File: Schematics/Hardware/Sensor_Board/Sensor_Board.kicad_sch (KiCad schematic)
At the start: 90 parts, among them J3 Conn_01x14

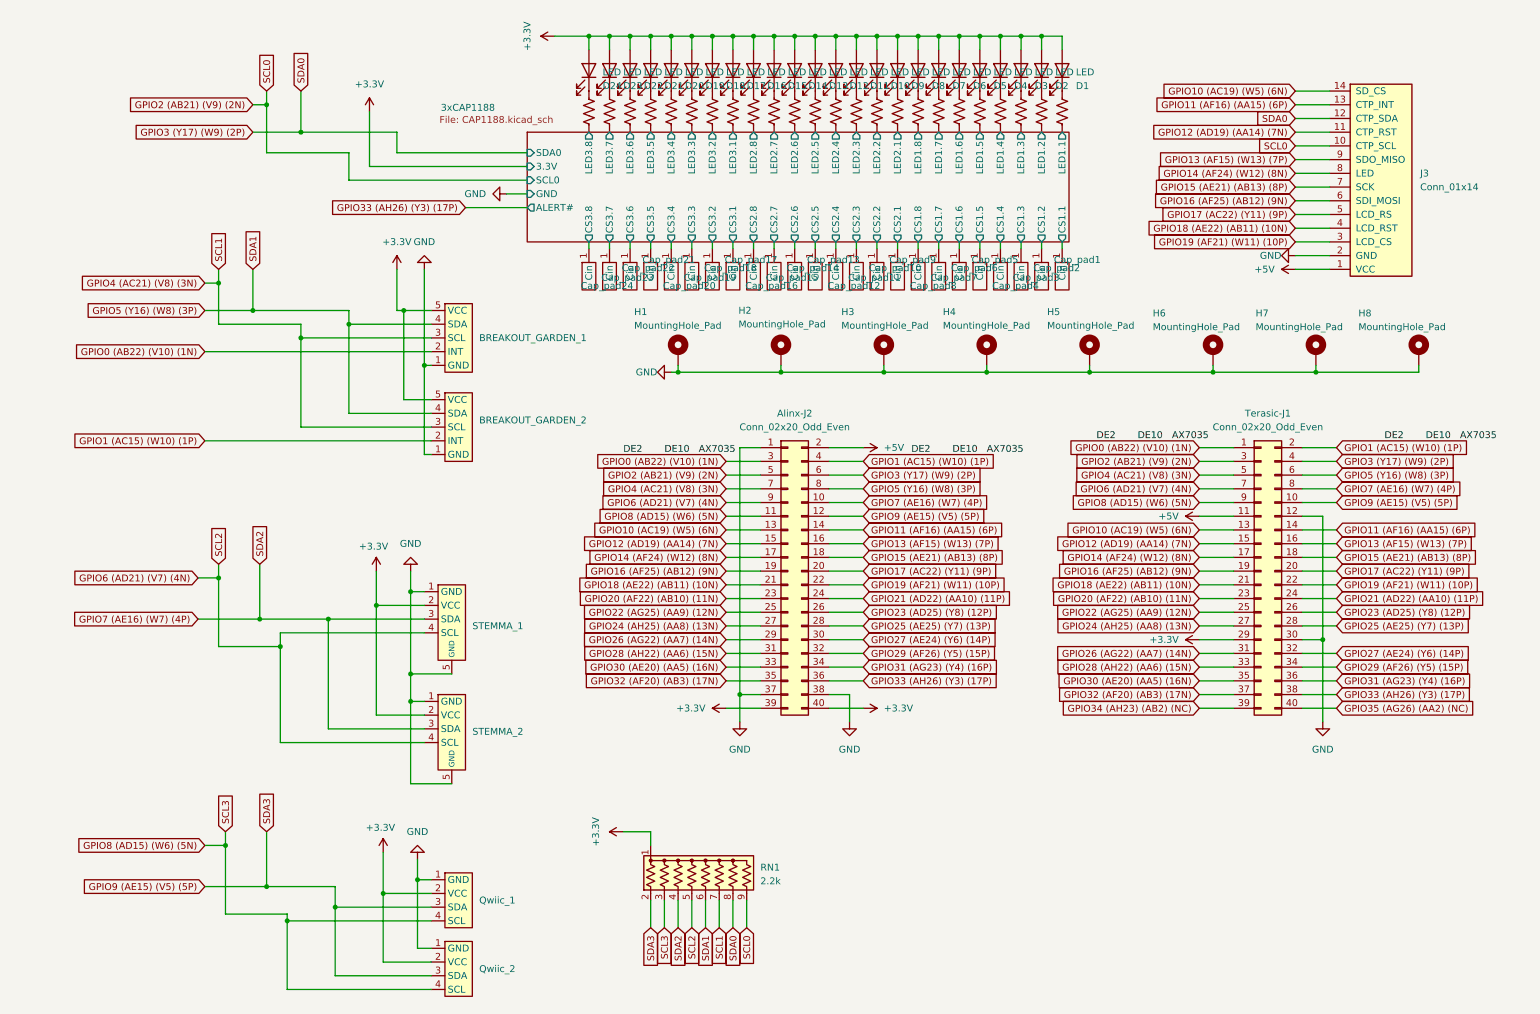
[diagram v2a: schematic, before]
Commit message: Final Final v0.5 sensor board PCB layout
Fixed incorrect Qwiic and Stemma pinouts.
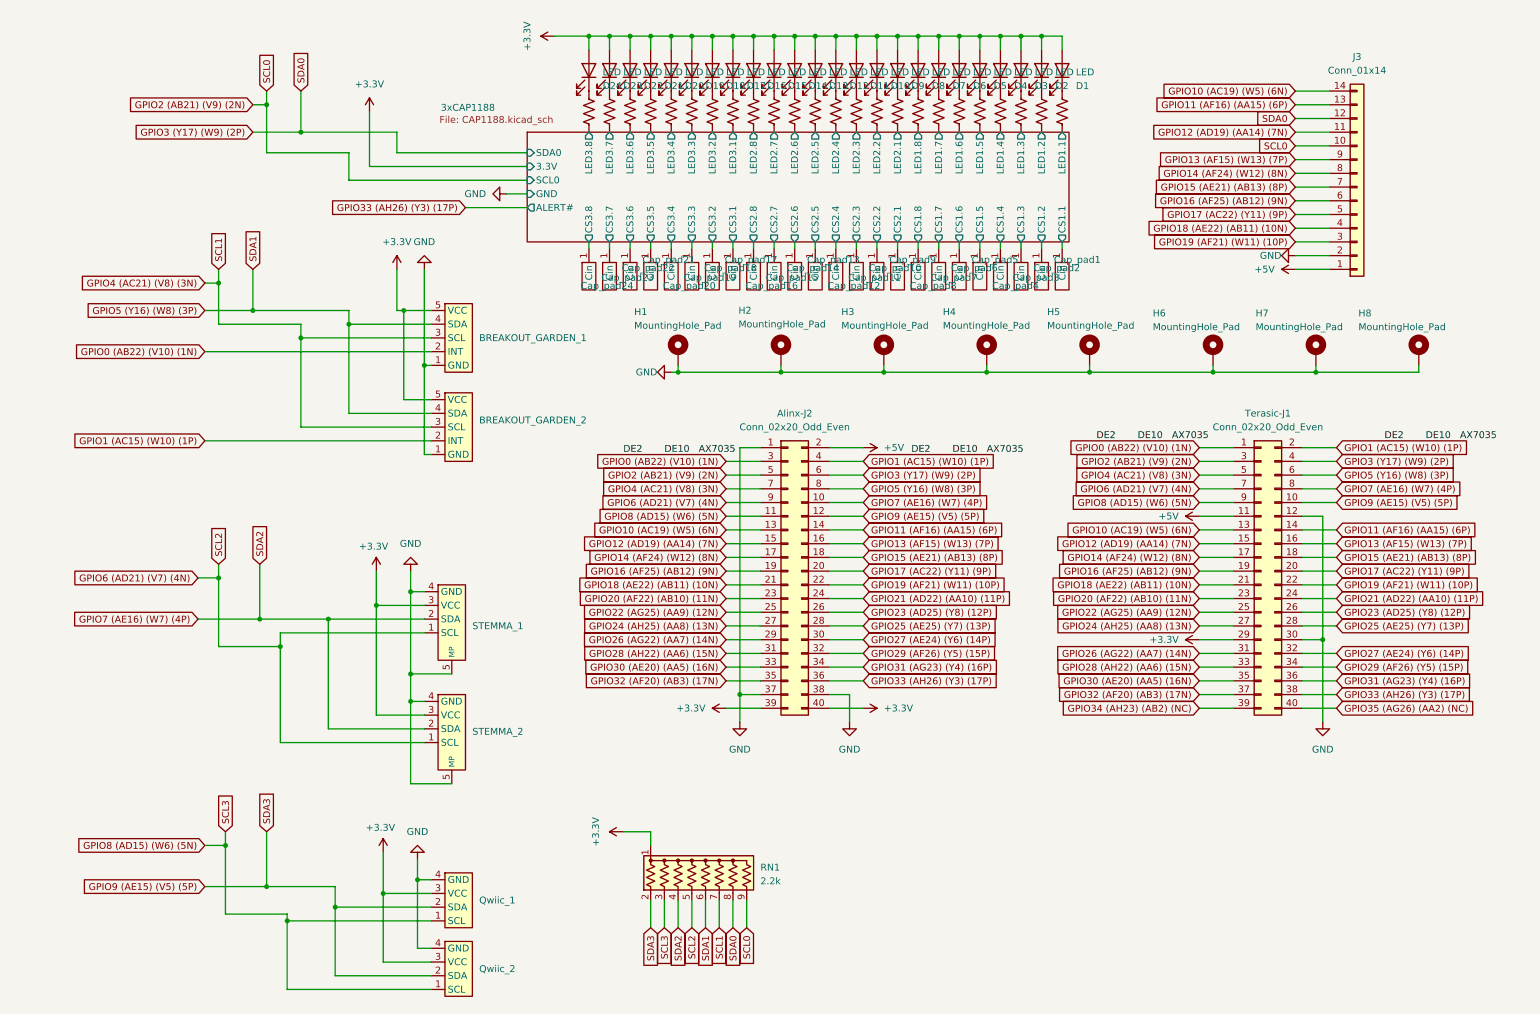
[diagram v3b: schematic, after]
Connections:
- net +3.3V: now also Qwiic_1.3 (VCC), Qwiic_2.3 (VCC), STEMMA_1.3 (VCC), STEMMA_2.3 (VCC); no longer Qwiic_1.2 (VCC), Qwiic_2.2 (VCC), STEMMA_1.2 (VCC), STEMMA_2.2 (VCC)
- net GND: now also Qwiic_1.4 (GND), Qwiic_2.4 (GND), STEMMA_1.4 (GND), STEMMA_2.4 (GND); no longer Qwiic_1.1 (GND), Qwiic_2.1 (GND), STEMMA_1.1 (GND), STEMMA_2.1 (GND)
- net GPIO6 (AD21) (V7) (4N): now also STEMMA_1.1 (SCL), STEMMA_2.1 (SCL); no longer STEMMA_1.4 (SCL), STEMMA_2.4 (SCL)
- net GPIO7 (AE16) (W7) (4P): now also STEMMA_1.2 (SDA), STEMMA_2.2 (SDA); no longer STEMMA_1.3 (SDA), STEMMA_2.3 (SDA)
- net GPIO8 (AD15) (W6) (5N): now also Qwiic_1.1 (SCL), Qwiic_2.1 (SCL); no longer Qwiic_1.4 (SCL), Qwiic_2.4 (SCL)
- net GPIO9 (AE15) (V5) (5P): now also Qwiic_1.2 (SDA), Qwiic_2.2 (SDA); no longer Qwiic_1.3 (SDA), Qwiic_2.3 (SDA)
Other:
- moved on the sheet: J3
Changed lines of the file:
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@@
 	)
 	(junction
+		(at 76.2 121.92)
+		(diameter 0)
+		(color 0 0 0 0)
+	)
+	(junction
 		(at 180.34 16.51)
 		(diameter 0)
@@
 	)
 	(junction
-		(at 82.55 119.38)
-		(diameter 0)
-		(color 0 0 0 0)
-	)
-	(junction
 		(at 77.47 175.26)
 		(diameter 0)
@@
 	)
 	(junction
-		(at 76.2 121.92)
-		(diameter 0)
-		(color 0 0 0 0)
-	)
-	(junction
 		(at 85.09 77.47)
 		(diameter 0)
@@
 	)
 	(junction
-		(at 67.31 124.46)
+		(at 82.55 134.62)
 		(diameter 0)
 		(color 0 0 0 0)
 	)
 	(junction
-		(at 82.55 134.62)
+		(at 161.29 16.51)
 		(diameter 0)
 		(color 0 0 0 0)
 	)
 	(junction
-		(at 161.29 16.51)
+		(at 168.91 16.51)
 		(diameter 0)
 		(color 0 0 0 0)
 	)
 	(junction
-		(at 168.91 16.51)
+		(at 67.31 124.46)
 		(diameter 0)
 		(color 0 0 0 0)
@@
 	)
 	(junction
+		(at 82.55 119.38)
+		(diameter 0)
+		(color 0 0 0 0)
+	)
+	(junction
 		(at 119.38 16.51)
 		(diameter 0)
@@
 	(wire
 		(pts
-			(xy 76.2 121.92) (xy 76.2 142.24)
+			(xy 228.6 118.11) (xy 234.95 118.11)
 		)
 		(stroke
@@
 	(wire
 		(pts
-			(xy 228.6 118.11) (xy 234.95 118.11)
+			(xy 130.81 78.74) (xy 132.08 78.74)
 		)
 		(stroke
@@
 	(wire
 		(pts
-			(xy 130.81 78.74) (xy 132.08 78.74)
+			(xy 80.01 59.69) (xy 80.01 67.31)
 		)
 		(stroke
@@
 	(wire
 		(pts
-			(xy 80.01 59.69) (xy 80.01 67.31)
+			(xy 67.31 124.46) (xy 85.09 124.46)
 		)
 		(stroke
@@
 	(wire
 		(pts
-			(xy 67.31 124.46) (xy 85.09 124.46)
-		)
-		(stroke
-			(width 0)
-			(type default)
-		)
-	)
-	(wire
-		(pts
 			(xy 160.02 107.95) (xy 166.37 107.95)
 		)
@@
 	(wire
 		(pts
-			(xy 58.42 127) (xy 85.09 127)
+			(xy 139.7 181.61) (xy 139.7 176.53)
 		)
 		(stroke
@@
 	(wire
 		(pts
-			(xy 139.7 181.61) (xy 139.7 176.53)
+			(xy 85.09 77.47) (xy 86.36 77.47)
 		)
 		(stroke
@@
 	(wire
 		(pts
-			(xy 85.09 77.47) (xy 86.36 77.47)
+			(xy 247.65 105.41) (xy 251.46 105.41)
 		)
 		(stroke
@@
 	(wire
 		(pts
-			(xy 247.65 105.41) (xy 251.46 105.41)
+			(xy 62.23 26.67) (xy 62.23 34.29)
 		)
 		(stroke
@@
 	(wire
 		(pts
-			(xy 62.23 26.67) (xy 62.23 34.29)
+			(xy 115.57 16.51) (xy 119.38 16.51)
 		)
 		(stroke
@@
 	(wire
 		(pts
-			(xy 115.57 16.51) (xy 119.38 16.51)
+			(xy 246.38 46.99) (xy 252.73 46.99)
 		)
 		(stroke
@@
 	(wire
 		(pts
-			(xy 246.38 46.99) (xy 252.73 46.99)
+			(xy 76.2 121.92) (xy 85.09 121.92)
 		)
 		(stroke
@@
 	(wire
 		(pts
+			(xy 82.55 115.57) (xy 82.55 119.38)
+		)
+		(stroke
+			(width 0)
+			(type default)
+		)
+	)
+	(wire
+		(pts
 			(xy 228.6 113.03) (xy 234.95 113.03)
 		)
@@
 	(wire
 		(pts
+			(xy 82.55 119.38) (xy 85.09 119.38)
+		)
+		(stroke
+			(width 0)
+			(type default)
+		)
+	)
+	(wire
+		(pts
 			(xy 140.97 115.57) (xy 147.32 115.57)
 		)
@@
 	(wire
 		(pts
+			(xy 58.42 127) (xy 85.09 127)
+		)
+		(stroke
+			(width 0)
+			(type default)
+		)
+	)
+	(wire
+		(pts
 			(xy 119.38 16.51) (xy 123.19 16.51)
 		)
@@
 	(wire
 		(pts
+			(xy 76.2 121.92) (xy 76.2 142.24)
+		)
+		(stroke
+			(width 0)
+			(type default)
+		)
+	)
+	(wire
+		(pts
 			(xy 228.6 100.33) (xy 234.95 100.33)
 		)
@@
 	(wire
 		(pts
-			(xy 76.2 121.92) (xy 85.09 121.92)
-		)
-		(stroke
-			(width 0)
-			(type default)
-		)
-	)
-	(wire
-		(pts
 			(xy 132.08 78.74) (xy 151.13 78.74)
 		)
@@
 	(wire
 		(pts
-			(xy 82.55 119.38) (xy 85.09 119.38)
-		)
-		(stroke
-			(width 0)
-			(type default)
-		)
-	)
-	(wire
-		(pts
 			(xy 77.47 187.96) (xy 86.36 187.96)
 		)
@@
 	(wire
 		(pts
-			(xy 80.01 67.31) (xy 81.28 67.31)
+			(xy 76.2 115.57) (xy 76.2 121.92)
 		)
 		(stroke
@@
 	(wire
 		(pts
-			(xy 59.69 180.34) (xy 59.69 193.04)
+			(xy 80.01 67.31) (xy 81.28 67.31)
 		)
 		(stroke
@@
 	(wire
 		(pts
-			(xy 127 16.51) (xy 127 19.05)
+			(xy 59.69 180.34) (xy 59.69 193.04)
 		)
 		(stroke
@@
 	(wire
 		(pts
-			(xy 86.36 185.42) (xy 83.82 185.42)
+			(xy 127 16.51) (xy 127 19.05)
 		)
 		(stroke
@@
 	(wire
 		(pts
-			(xy 82.55 115.57) (xy 82.55 119.38)
+			(xy 86.36 185.42) (xy 83.82 185.42)
 		)
 		(stroke
@@
 	(wire
 		(pts
-			(xy 76.2 115.57) (xy 76.2 121.92)
+			(xy 246.38 39.37) (xy 252.73 39.37)
 		)
 		(stroke
@@
 	(wire
 		(pts
-			(xy 246.38 39.37) (xy 252.73 39.37)
+			(xy 82.55 119.38) (xy 82.55 134.62)
 		)
 		(stroke
@@
 	(wire
 		(pts
-			(xy 82.55 119.38) (xy 82.55 134.62)
-		)
-		(stroke
-			(width 0)
-			(type default)
-		)
-	)
-	(wire
-		(pts
 			(xy 228.6 115.57) (xy 234.95 115.57)
 		)
@@
 	(symbol
 		(lib_id "Connector_Generic:Conn_01x14")
-		(at 260.35 41.91 0)
+		(at 257.81 44.45 0)
+		(mirror x)
 		(unit 1)
 		(exclude_from_sim no)
@@
 		(on_board yes)
 		(dnp no)
-		(fields_autoplaced yes)
 		(property "Reference" "J3"
-			(at 269.494 41.91 0)
+			(at 257.81 20.32 0)
 			(effects
 				(font
 					(size 1.27 1.27)
 				)
-				(justify left)
 			)
 		)
 		(property "Value" "Conn_01x14"
-			(at 269.494 44.45 0)
+			(at 257.81 22.86 0)
 			(effects
 				(font
 					(size 1.27 1.27)
 				)
-				(justify left)
 			)
 		)
 		(property "Footprint" "Connector_PinSocket_2.54mm:PinSocket_1x14_P2.54mm_Vertical"
-			(at 260.35 41.91 0)
+			(at 257.81 44.45 0)
 			(effects
 				(font
@@
 		)
 		(property "Datasheet" "~"
-			(at 260.35 41.91 0)
+			(at 257.81 44.45 0)
 			(effects
 				(font
@@
 		)
 		(property "Description" "Generic connector, single row, 01x14, script generated (kicad-library-utils/schlib/autogen/connector/)"
-			(at 260.35 41.91 0)
+			(at 257.81 44.45 0)
 			(effects
 				(font

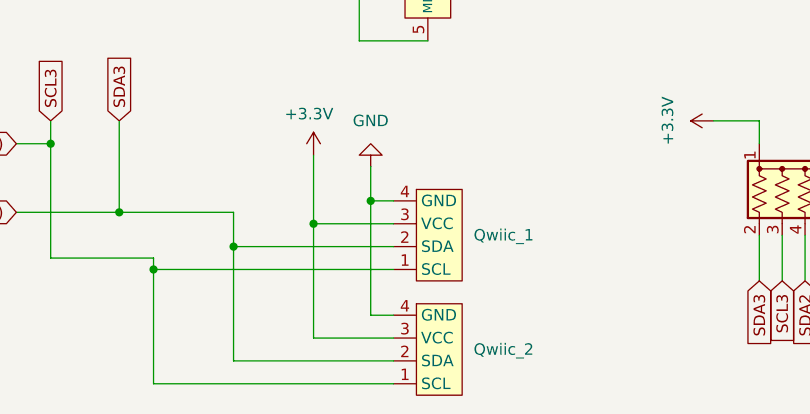
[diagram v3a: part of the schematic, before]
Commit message: v0.7 Sensor Board Files
Fixed LCD footprint to now include GND.
Fixed Qwiic connector pinout.
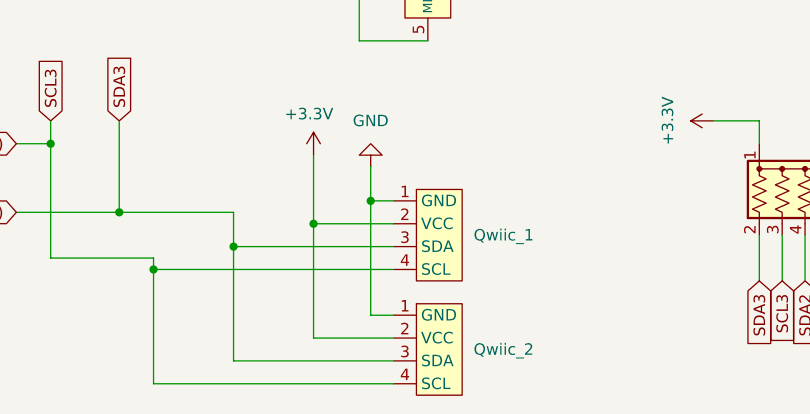
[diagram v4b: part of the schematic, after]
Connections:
- net +3.3V: now also Qwiic_1.2 (VCC), Qwiic_2.2 (VCC); no longer Qwiic_1.3 (VCC), Qwiic_2.3 (VCC)
- net GND: now also Qwiic_1.1 (GND), Qwiic_2.1 (GND); no longer Qwiic_1.4 (GND), Qwiic_2.4 (GND)
- net GPIO8 (AD15) (W6) (5N): now also Qwiic_1.4 (SCL), Qwiic_2.4 (SCL); no longer Qwiic_1.1 (SCL), Qwiic_2.1 (SCL)
- net GPIO9 (AE15) (V5) (5P): now also Qwiic_1.3 (SDA), Qwiic_2.3 (SDA); no longer Qwiic_1.2 (SDA), Qwiic_2.2 (SDA)
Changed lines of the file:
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@@
 	(paper "A4")
 	(title_block
-		(date "2026-03-18")
-		(rev "0.5")
+		(date "2026-04-24")
+		(rev "0.7")
 	)
 	(junction
